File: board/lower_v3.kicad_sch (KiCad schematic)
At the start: 17 parts, among them J1 To Power Bank, J10 PIN_RING_MOTOR, J11 PIN_PINKY_MOTOR, J12 PIN_PINKY_SPLAY, J13 PIN_RING_SPLAY, J14 PIN_MIDDLE_SPLAY, J15 PIN_INDEX_SPLAY, J16 PIN_THUMB_SPLAY, J2 PIN_PINKY, J3 PIN_RING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

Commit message: Finalize board
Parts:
- added J17: PIN_A_BTN, Connector_PinHeader_2.54mm:PinHeader_1x02_P2.54mm_Vertical, symbol Connector:Conn_01x02_Male
- added J18: PIN_B_BTN, Connector_PinHeader_2.54mm:PinHeader_1x02_P2.54mm_Vertical, symbol Connector:Conn_01x02_Male
- added J19: JOYSTICK, Connector_PinHeader_2.54mm:PinHeader_1x05_P2.54mm_Vertical, symbol Connector:Conn_01x05_Male
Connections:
- net GND: now also J17.2 (Pin_2), J18.2 (Pin_2), J19.1 (Pin_1)
- net at J15.1 (Pin_1): now also U1.18 (D12); no longer U1.16 (D27)
- net at J1.2 (Pin_2), J10.2 (Pin_2), J11.2 (Pin_2)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: now also J19.3 (Pin_3)
- net at U1.13 (D33): now also J19.5 (Pin_5); no longer J12.1 (Pin_1)
- net at U1.14 (D25): now also J19.4 (Pin_4); no longer J13.1 (Pin_1)
- net at U1.15 (D26): now also J12.1 (Pin_1); no longer J14.1 (Pin_1)
- net at U1.17 (D14): now also J14.1 (Pin_1); no longer J16.1 (Pin_1)
- net at U1.20 (D13): now also J16.1 (Pin_1)
- net at U1.36 (D23): now also J17.1 (Pin_1)
- net at U1.39 (D22): now also J18.1 (Pin_1)
- net at U1.41 (D1): now also J19.2 (Pin_2)
- new net: J13.1 (Pin_1), U1.16 (D27)

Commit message: Rev C
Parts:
- removed J1: To Power Bank, Connector_PinHeader_2.54mm:PinHeader_1x03_P2.54mm_Vertical, symbol Connector:Conn_01x03_Male
- added J1: POWER, Connector_JST:JST_EH_S4B-EH_1x04_P2.50mm_Horizontal, symbol Connector:Conn_01x04_Female
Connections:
- net GND: now also J19.4 (Pin_4), U1.102 (GND), J1.1 (Pin_1), J1.4 (Pin_4); no longer J19.1 (Pin_1)
- net 3V3: now reaches J12.2 (Pin_2), J13.2 (Pin_2), J14.2 (Pin_2), J15.2 (Pin_2), J16.2 (Pin_2), J2.2 (Pin_2), J3.2 (Pin_2), J4.2 (Pin_2), J5.2 (Pin_2), J6.2 (Pin_2)
- net 3V3: now also J19.1 (Pin_1), J1.2 (Pin_2); no longer U1.104 (3V3)
- net 5V: now reaches J10.2 (Pin_2), J11.2 (Pin_2), J7.2 (Pin_2), J8.2 (Pin_2), J9.2 (Pin_2), U1.103 (VIN)
- net 5V: now also J1.3 (Pin_3); no longer J19.3 (Pin_3)
- net at U1.14 (D25): now also J19.2 (Pin_2); no longer J19.4 (Pin_4)
- net Net-(U1-Pad20): now reaches J16.1 (Pin_1), U1.20 (D13)
- net at U1.36 (D23): now also J18.1 (Pin_1); no longer J17.1 (Pin_1)
- net at U1.39 (D22): now also J17.1 (Pin_1); no longer J18.1 (Pin_1)
- net at U1.41 (D1): now also J19.3 (Pin_3); no longer J19.2 (Pin_2)
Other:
- note added: "3V3"
- note added: "BTN"
- note added: "GND"
- note added: "PIN_JOY_X"
- note added: "PIN_JOY_Y"
- moved on the sheet: J17, J18, J19

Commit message: Locate OpAmp and Photo Diodes
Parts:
- added D? (x3): BPV22NF, XDCR_BPV22NF, symbol BPV22NF:BPV22NF
- added U2: TLV2462IP, DIP794W45P254L959H508Q8, symbol TLV2462IP:TLV2462IP
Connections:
- new net: D?.A, D?.A, D?.A
- new net: D?.K, D?.K, D?.K
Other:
- moved on the sheet: J1, J10, J11, J12, J13, J14, J15, J16, J17, J18, J19, J2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

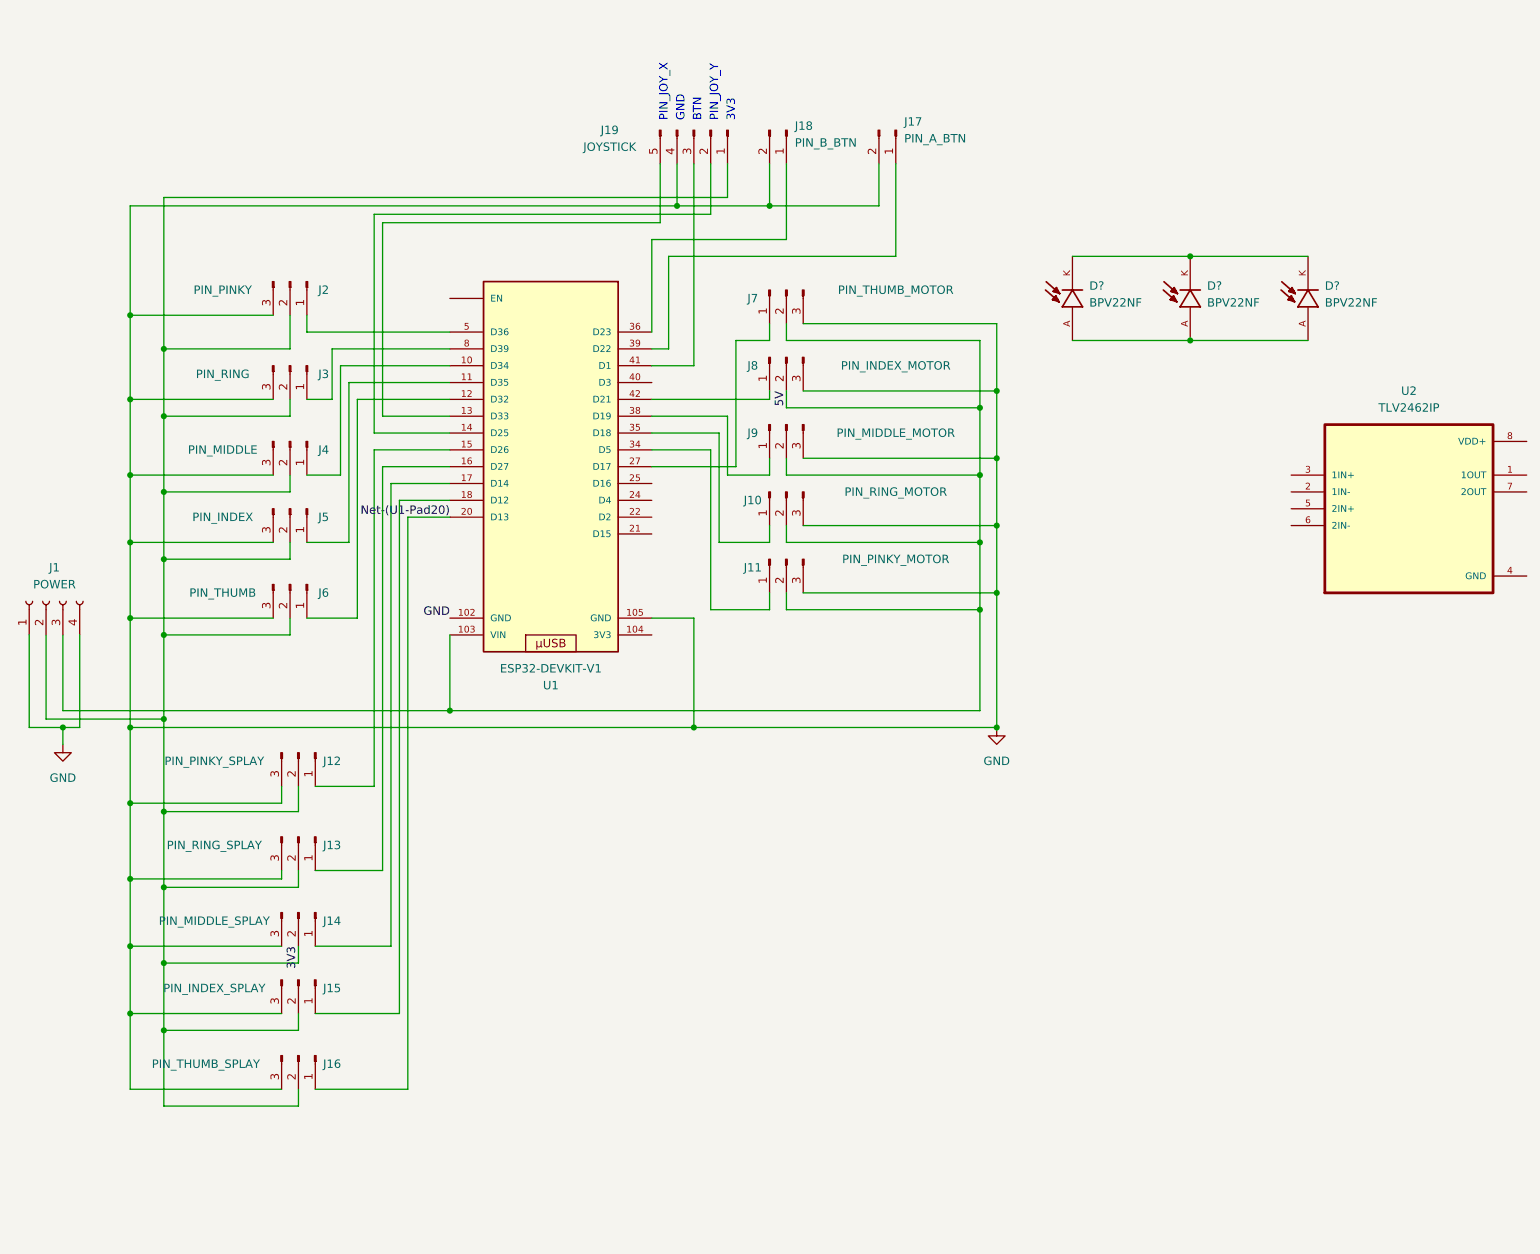
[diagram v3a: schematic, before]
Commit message: Combine joystick connector, add C and R
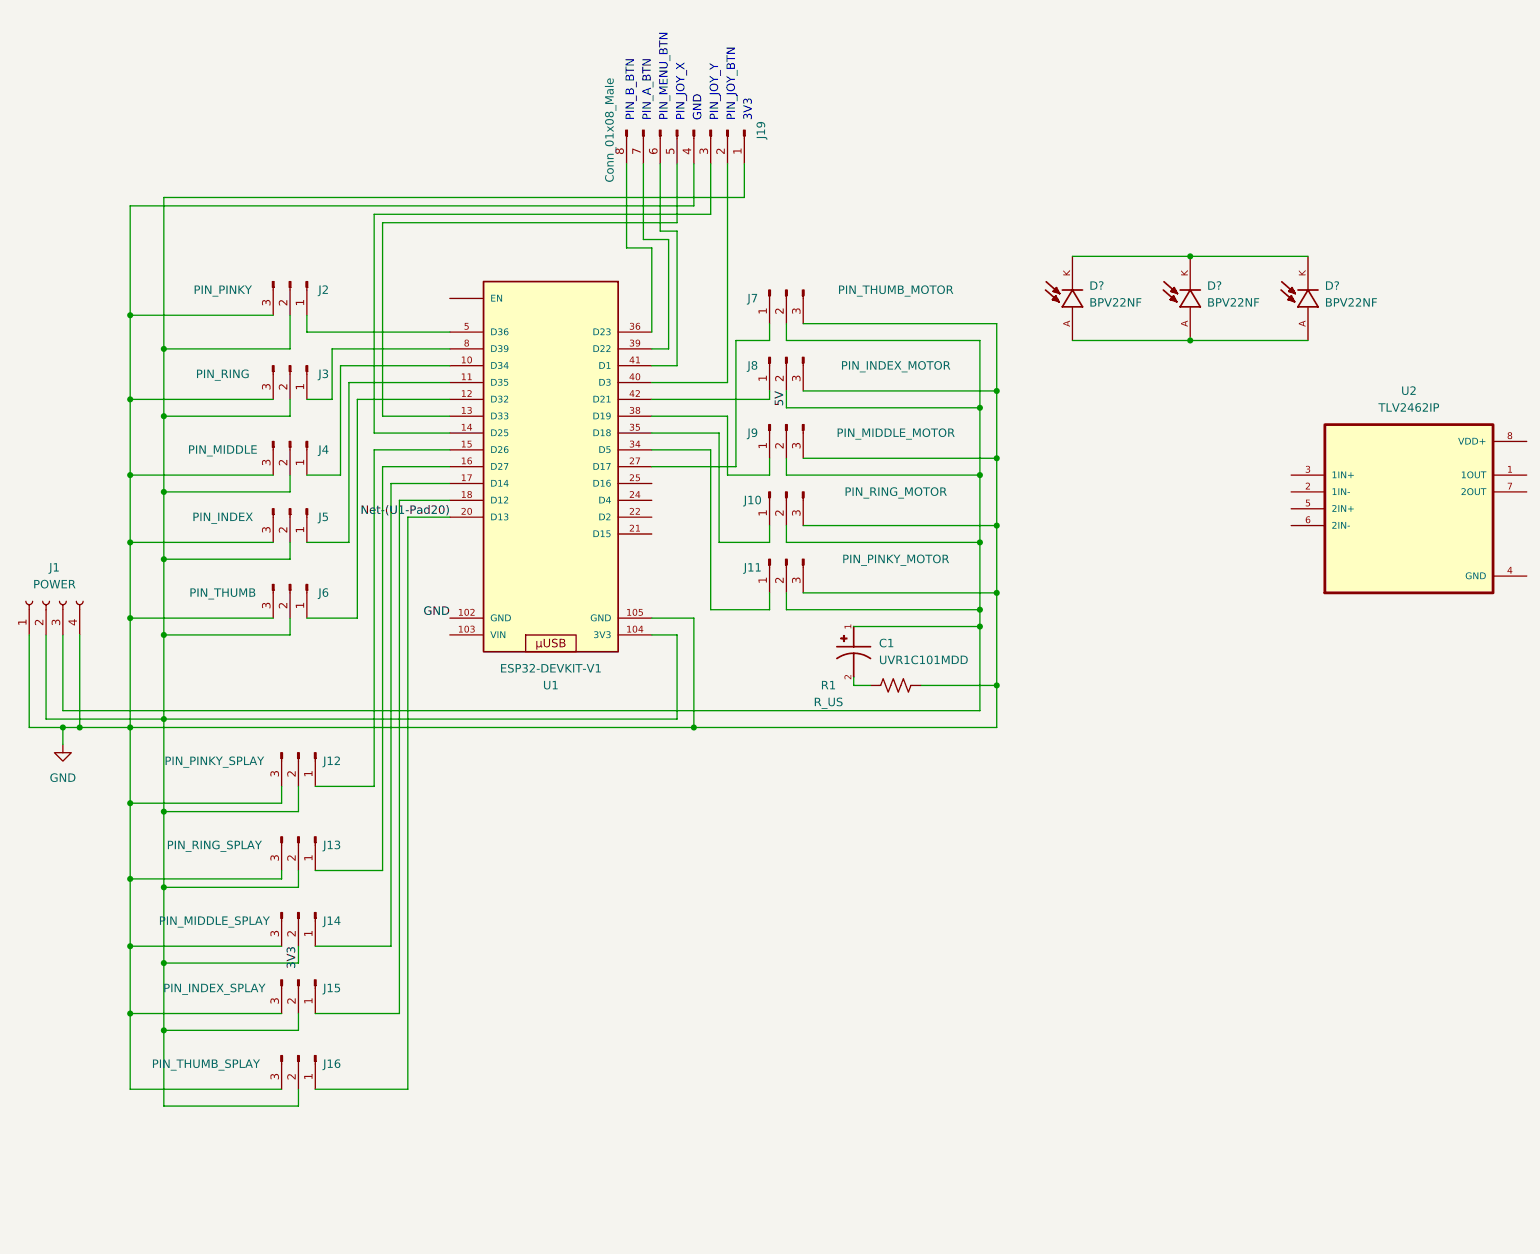
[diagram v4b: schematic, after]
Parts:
- removed J17: PIN_A_BTN, Connector_PinHeader_2.54mm:PinHeader_1x02_P2.54mm_Vertical, symbol Connector:Conn_01x02_Male
- removed J18: PIN_B_BTN, Connector_PinHeader_2.54mm:PinHeader_1x02_P2.54mm_Vertical, symbol Connector:Conn_01x02_Male
- added C1: UVR1C101MDD, UVR1C101MDD:CAPPRD200W50D550H1250, symbol UVR1C101MDD:UVR1C101MDD
- added R1: R_US, Resistor_THT:R_Axial_DIN0309_L9.0mm_D3.2mm_P12.70mm_Horizontal, symbol Device:R_US
- J19: value JOYSTICK -> Conn_01x08_Male; symbol Connector:Conn_01x05_Male -> Connector:Conn_01x08_Male
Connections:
- net 3V3: now also U1.104 (3V3)
- net 5V: now also C1.1; no longer U1.103 (VIN)
- net GND: now also R1.1
- net at U1.14 (D25): now also J19.3 (Pin_3); no longer J19.2 (Pin_2)
- net at U1.36 (D23): now also J19.8 (Pin_8)
- net at U1.39 (D22): now also J19.7 (Pin_7)
- net at U1.40 (D3): now also J19.2 (Pin_2)
- net at U1.41 (D1): now also J19.6 (Pin_6); no longer J19.3 (Pin_3)
- new net: C1.2, R1.2
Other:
- note added: "PIN_A_BTN"
- note added: "PIN_B_BTN"
- note added: "PIN_JOY_BTN"
- note added: "PIN_MENU_BTN"
- note removed: "BTN"

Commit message: RevC RC 1
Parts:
- removed C1: UVR1C101MDD, UVR1C101MDD:CAPPRD200W50D550H1250, symbol UVR1C101MDD:UVR1C101MDD
- removed D? (x3): BPV22NF, XDCR_BPV22NF, symbol BPV22NF:BPV22NF
- removed U2: TLV2462IP, DIP794W45P254L959H508Q8, symbol TLV2462IP:TLV2462IP
- added C1: C_Polarized, Capacitor_THT:CP_Radial_D10.0mm_P5.00mm, symbol Device:C_Polarized
- J1: footprint Connector_JST:JST_EH_S4B-EH_1x04_P2.50mm_Horizontal -> Connector_JST:JST_EH_B4B-EH-A_1x04_P2.50mm_Vertical
- J19: footprint Connector_PinHeader_2.54mm:PinHeader_1x05_P2.54mm_Vertical -> Connector_PinSocket_2.54mm:PinSocket_2x04_P2.54mm_Vertical
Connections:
- net 5V: now also C1.1
- net GND: no longer U1.102 (GND)
- net Net-(U1-Pad20): no longer J16.1 (Pin_1)
- net at J15.1 (Pin_1): now also U1.16 (D27); no longer U1.18 (D12)
- net at J11.1 (Pin_1): now also U1.27 (D17); no longer U1.34 (D5)
- net at U1.13 (D33): now also J12.1 (Pin_1); no longer J19.5 (Pin_5)
- net at U1.14 (D25): now also J13.1 (Pin_1); no longer J19.3 (Pin_3)
- net at U1.15 (D26): now also J14.1 (Pin_1); no longer J12.1 (Pin_1)
- net at U1.17 (D14): now also J16.1 (Pin_1); no longer J14.1 (Pin_1)
- net at U1.21 (D15): now also J7.1 (Pin_1)
- net at U1.22 (D2): now also J8.1 (Pin_1)
- net at U1.24 (D4): now also J9.1 (Pin_1)
- net at U1.25 (D16): now also J10.1 (Pin_1)
- net at U1.35 (D18): no longer J10.1 (Pin_1)
- net at U1.38 (D19): now also J19.6 (Pin_6); no longer J9.1 (Pin_1)
- net at U1.40 (D3): now also J19.3 (Pin_3); no longer J19.2 (Pin_2)
- net at U1.41 (D1): now also J19.2 (Pin_2); no longer J19.6 (Pin_6)
- net at U1.42 (D21): now also J19.5 (Pin_5); no longer J8.1 (Pin_1)
- net at R1.2: now also C1.2
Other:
- moved on the sheet: J19, J9, R1

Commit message: Smallerize resistor
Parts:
- R1: footprint Resistor_THT:R_Axial_DIN0309_L9.0mm_D3.2mm_P12.70mm_Horizontal -> Resistor_THT:R_Axial_DIN0207_L6.3mm_D2.5mm_P10.16mm_Horizontal
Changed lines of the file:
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@@
     (property "Reference" "R1" (id 0) (at 142.24 109.22 90))
     (property "Value" "R_US" (id 1) (at 142.24 111.76 90))
-    (property "Footprint" "Resistor_THT:R_Axial_DIN0309_L9.0mm_D3.2mm_P12.70mm_Horizontal" (id 2) (at 152.146 110.236 90)
+    (property "Footprint" "Resistor_THT:R_Axial_DIN0207_L6.3mm_D2.5mm_P10.16mm_Horizontal" (id 2) (at 152.146 110.236 90)
       (effects (font (size 1.27 1.27)) hide)
     )
@@
     )
     (path "/7aaf189b-37e0-4195-b868-1caa4b00585d"
-      (reference "R1") (unit 1) (value "R_US") (footprint "Resistor_THT:R_Axial_DIN0309_L9.0mm_D3.2mm_P12.70mm_Horizontal")
+      (reference "R1") (unit 1) (value "R_US") (footprint "Resistor_THT:R_Axial_DIN0207_L6.3mm_D2.5mm_P10.16mm_Horizontal")
     )
     (path "/2759ef2b-fb73-4f9c-b218-914252ad87a7"
